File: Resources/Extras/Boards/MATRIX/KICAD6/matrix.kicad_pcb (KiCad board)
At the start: 2 copper layers, 134.6 x 90.8 mm, 34 parts, among them J1 Conn_01x24, J2 Conn_01x24, J3 Conn_01x24, J4 Conn_01x24, U1 Teensy4.1

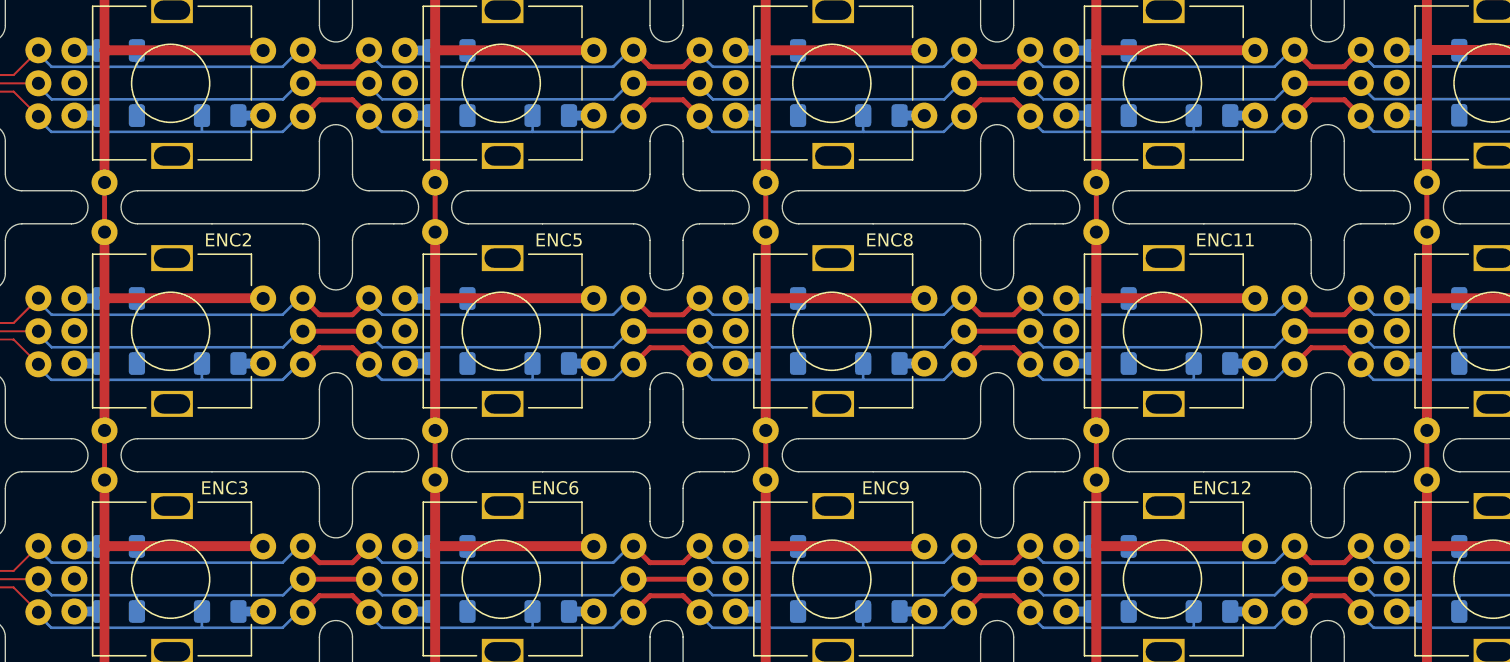
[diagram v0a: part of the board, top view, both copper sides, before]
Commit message: Fixed errors in matrix test board
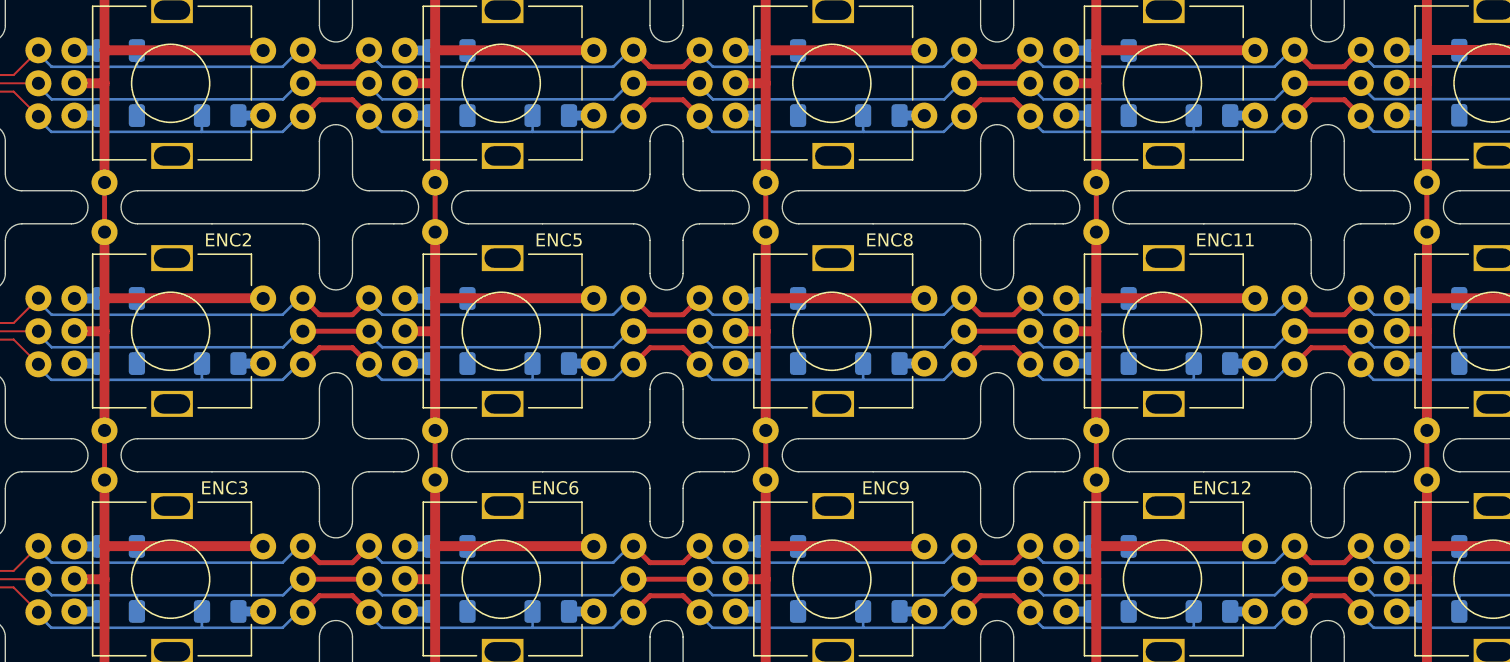
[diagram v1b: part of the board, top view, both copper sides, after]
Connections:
- J3 pad 11: /SR3 -> /BR3
- J3 pad 12: /BR3 -> /SR3
- J3 pad 5: /SR0 -> /BR0
- J3 pad 6: /BR0 -> /SR0
- J3 pad 8: /SR1 -> /BR1
- J3 pad 9: /BR1 -> /SR1
- J4 pad 11: /SR3 -> /BR3
- J4 pad 12: /BR3 -> /SR3
- J4 pad 5: /SR0 -> /BR0
- J4 pad 6: /BR0 -> /SR0
- J4 pad 8: /SR1 -> /BR1
- J4 pad 9: /BR1 -> /SR1
- U1 pad 11: /SR3 -> /BR3
- U1 pad 12: /BR3 -> /SR3
- U1 pad 5: /SR0 -> /BR0
- U1 pad 6: /BR0 -> /SR0
- U1 pad 8: /SR1 -> /BR1
- U1 pad 9: /BR1 -> /SR1
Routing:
- net /SR3: track 79.9 -> 81.9 mm
- net /BR3: track 81.9 -> 79.9 mm
- net /SR1: track 94.4 -> 96.4 mm
- net /BR1: track 96.4 -> 94.4 mm
- net /SR0: track 108.6 -> 110.5 mm
- net /BR0: track 110.5 -> 108.6 mm
- net Net-(ENC6-PadS2): track 5.08 -> 6.13 mm
- net Net-(ENC6-PadB2): track 6.13 -> 5.08 mm
- net Net-(ENC5-PadS2): track 5.08 -> 6.13 mm
- net Net-(ENC5-PadB2): track 6.13 -> 5.08 mm
- net Net-(ENC12-PadS1): track 5.08 -> 6.13 mm
- net Net-(ENC12-PadB1): track 6.13 -> 5.08 mm
- net Net-(ENC11-PadS1): track 5.08 -> 6.13 mm
- net Net-(ENC11-PadB1): track 6.13 -> 5.08 mm
- net Net-(ENC4-PadS2): track 5.08 -> 6.13 mm
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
